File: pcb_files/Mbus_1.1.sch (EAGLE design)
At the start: 51 parts, among them IC1 NCP1117ST50T3G, IC3 ATMEGA2560-16AU, IC4 RTC_PCF8523T, J1 F-1X18-SIP-100-32Y, J2 USB_A_SMT_FEMALE, M1 SERVO, Q2 32.768, Y1 CSTCE16M0V53-R0 16MHZ

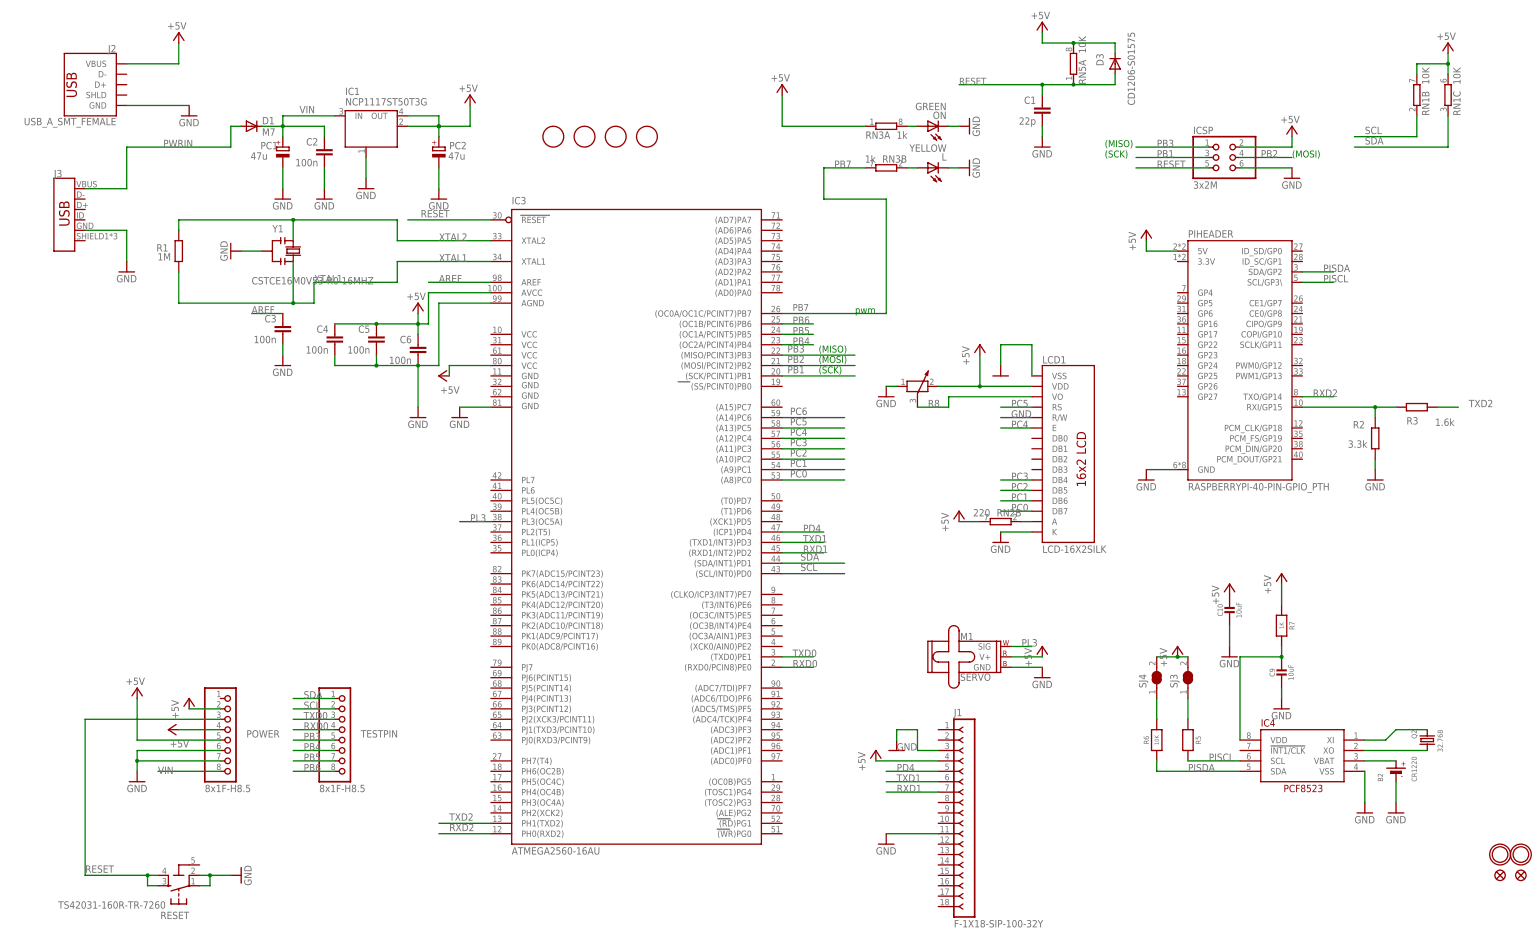
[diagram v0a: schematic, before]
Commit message: A second version based on the previous one with similar layout.
Signed-off-by: Yiteng Cai <alonsochate@umich.edu>
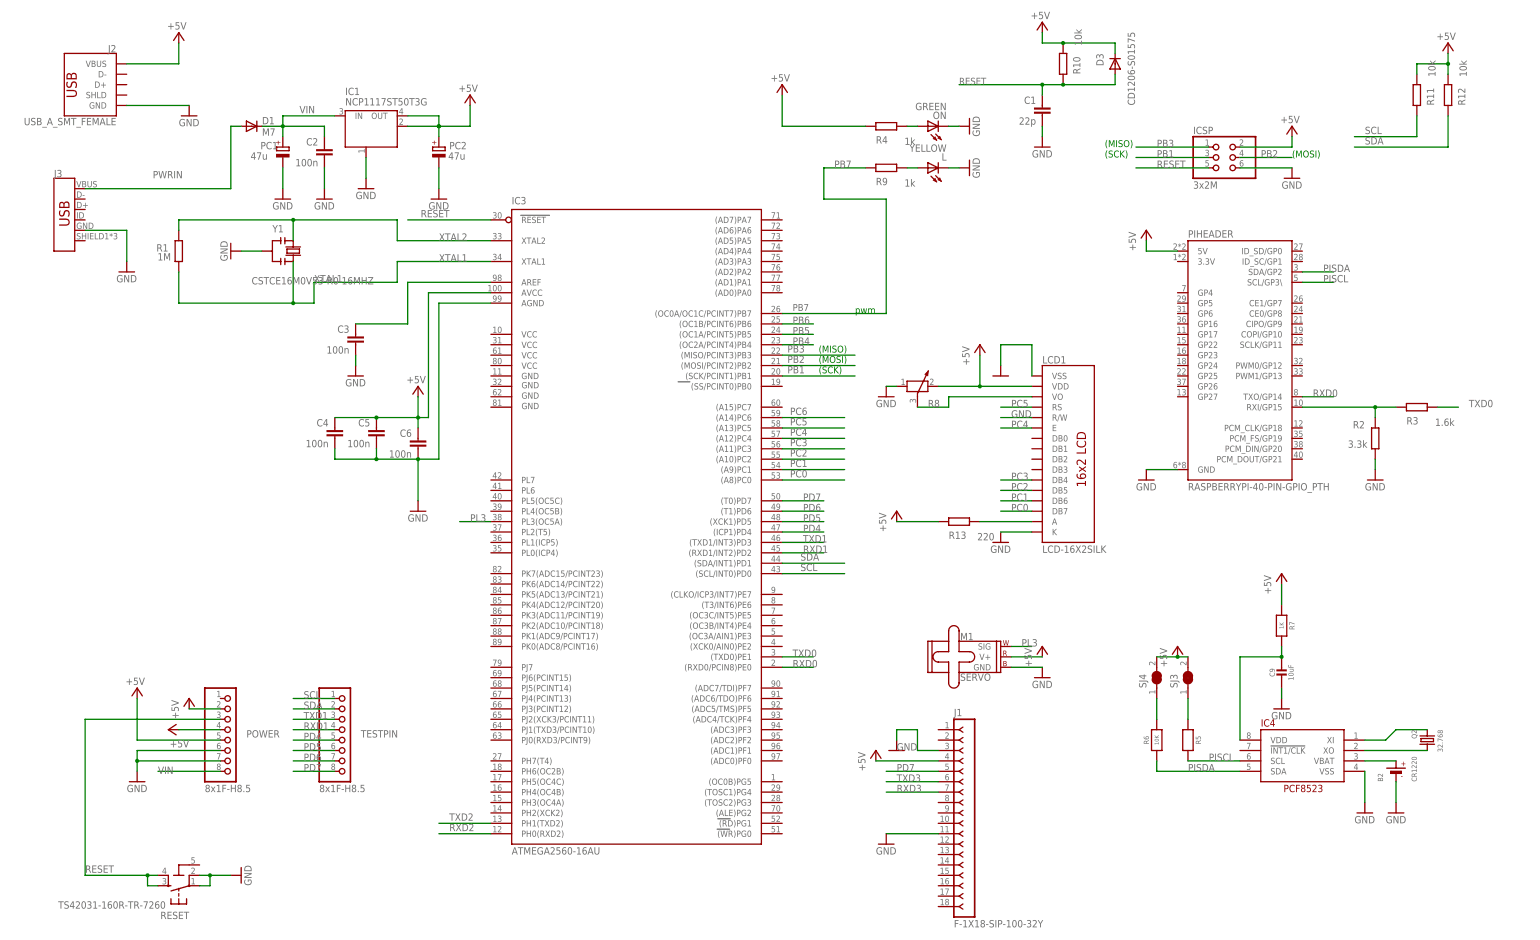
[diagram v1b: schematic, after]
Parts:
- removed C10: 10uF, microbuilder:CAP_CERAMIC0805-NOOUTLINE
- removed FD1, FD2, FD3, FD4: FIDUCIALMOUNT, SmartPrj:FIDUCIALMOUNT
- removed FID3, FID4: FIDUCIAL"", microbuilder:FIDUCIAL""
- removed RN1, RN5: 10K, resistor-dil:4R-NCAT16
- removed RN2: 220, resistor-dil:4R-NCAY16
- removed RN3: 1k, resistor-dil:4R-NCAY16
- removed U$2, U$3: MOUNTINGHOLE2.0, microbuilder:MOUNTINGHOLE2.0
- added R10, R11, R12: 10k, SmartPrj:R-EU_R0603
- added R13: 220, SmartPrj:R-EU_R0603
- added R4, R9: 1k, SmartPrj:R-EU_R0603
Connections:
- new net PD5: IC3.(XCK1)PD5, TESTPIN.6
- new net PD6: IC3.(T1)PD6, TESTPIN.7
- new net PD7: IC3.(T0)PD7, J1.5, TESTPIN.8
- new net RXD3: J1.7
- new net TXD3: J1.6
- net +5V: now also R10.1, R11.1, R12.1, R13.2, R4.2; no longer C10.1, IC3.VCC3, RN1B.2, RN1C.2, RN2B.2, RN3A.1, RN5A.2
- net GND: no longer C10.2, IC3.GND3
- net N$11: now also R13.1; no longer RN2B.1
- net N$2: now also R9.1; no longer RN3B.1
- net N$3: now also R4.1; no longer RN3A.2
- net PB3: no longer TESTPIN.5
- net PB4: no longer TESTPIN.6
- net PB5: no longer TESTPIN.7
- net PB6: no longer TESTPIN.8
- net PB7: now also R9.2; no longer RN3B.2
- net PD4: now also TESTPIN.5; no longer J1.5
- net RESET: now also R10.2; no longer RN5A.1
- net RXD0: now also PIHEADER.TXO/GP14; no longer TESTPIN.4
- net RXD1: now also TESTPIN.4; no longer J1.7
- net RXD2: no longer PIHEADER.TXO/GP14
- net SCL: now also R11.2, TESTPIN.1; no longer RN1B.1, TESTPIN.2
- net SDA: now also R12.2, TESTPIN.2; no longer RN1C.1, TESTPIN.1
- net TXD0: now also R3.1; no longer TESTPIN.3
- net TXD1: now also TESTPIN.3; no longer J1.6
- net TXD2: no longer R3.1
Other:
- moved on the sheet: C3, C4, C5, C6
